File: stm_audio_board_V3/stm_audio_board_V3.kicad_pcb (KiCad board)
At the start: 4 copper layers, 230.9 x 117 mm, 334 parts, among them J1 Power conn, J10 USB_A, J11 AudioJack_Loop1_Return, J12 AudioJack_Loop1_Send, J13 AudioJack_INPUT_Main, J14 AudioJack_OUTPUT_Main, J15 AudioJack_Loop2_Send, J16 STlink_DISP_MCU, J17 Conn_01x10_Footswitch, J18 USB3_A, J2 STlink_DSP, J3 Audio_sig, J4 Conn_01x01_taptempo, J5 Barrel_Jack_MountingPin, J6 Conn_01x03_pot_ext, J7 AudioJack_Loop3_Return, J8 AudioJack_Loop3_Send, J9 AudioJack_Loop2_Return, SW1 SW_SPST, SW2 SW_SPST, U1 IS42S16100H-7TL, U10 OP275, U12 OP275, U13 74HC14, U14 OP275, U15 STM32H723ZGTx, U2 OP275, U3 7909, U4 OP275, U5 MIC2920A-3.3WS-TR, U6 7809, U7 STM32H723ZGTx, U8 OP275, U9 MIC2920A-3.3WS-TR, Y1 X1E0000210132, Y2 X1E0000210132

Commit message: New orientation, Overvoltage protection added
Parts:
- removed C54, C55, C56, C57, C59, C61, C62: 100n, Capacitor_SMD:C_0603_1608Metric
- removed J18: USB3_A, Connector_USB:USB3_A_Receptacle_Wuerth_692122030100
- added C63: 100n, Capacitor_SMD:C_0603_1608Metric, F.Cu at (81.6, 126.1)
- added D1: 1N5819, Diode_SMD:D_SOD-323, F.Cu at (218.1, 82.8)
- added D12: 1N5819, Diode_SMD:D_SOD-323, F.Cu at (209.2, 79.0)
- added D13: 1N5819, Diode_SMD:D_SOD-323, F.Cu at (192.4, 84.8)
- added D14: 1N5819, Diode_SMD:D_SOD-323, F.Cu at (189.1, 84.8)
- added D15: 1N5819, Diode_SMD:D_SOD-323, F.Cu at (192.4, 82.8)
- added D16: 1N5819, Diode_SMD:D_SOD-323, F.Cu at (189.1, 82.8)
- added D17: 1N5819, Diode_SMD:D_SOD-323, F.Cu at (200.8, 82.0)
- added D18: 1N5819, Diode_SMD:D_SOD-323, F.Cu at (197.5, 82.0)
- added D19: 1N5819, Diode_SMD:D_SOD-323, F.Cu at (200.8, 80.0)
- added D20: 1N5819, Diode_SMD:D_SOD-323, F.Cu at (197.5, 80.0)
- added D4: 1N5819, Diode_SMD:D_SOD-323, F.Cu at (214.8, 82.8)
- added D5: 1N5819, Diode_SMD:D_SOD-323, F.Cu at (214.8, 80.8)
- added D6: 1N5819, Diode_SMD:D_SOD-323, F.Cu at (218.1, 80.8)
- added D7: 1N5819, Diode_SMD:D_SOD-323, F.Cu at (206.9, 82.4)
- added D8: 1N5819, Diode_SMD:D_SOD-323, F.Cu at (206.9, 79.1)
- added D9: 1N5819, Diode_SMD:D_SOD-323, F.Cu at (209.1, 82.4)
- added U16: USBLC6-2P6, Package_TO_SOT_SMD:SOT-666, F.Cu at (78.5, 126.1)
- moved C129 87.6 mm to (84.8, 91.9), turned to 180 degrees
- moved C131 82.2 mm to (85.0, 110.3), turned to 180 degrees
- moved C127 69.4 mm to (104.7, 92.1), turned to 180 degrees
- moved C130 62.7 mm to (105.1, 109.9), turned to 180 degrees
- moved C126 57.4 mm to (124.8, 92.0), turned to 180 degrees
- moved C78 54.0 mm to (170.0, 130.7), turned to -90 degrees
- moved C188 53.6 mm to (247.3, 128.9)
- moved C189 53.6 mm to (245.0, 121.6)
- moved J17 53.6 mm to (234.7, 142.4)
- moved R78 53.6 mm to (235.6, 124.7)
- moved C185 53.6 mm to (238.1, 122.5)
- moved C186 53.6 mm to (238.2, 125.6)
- moved C187 53.6 mm to (238.2, 129.2)
- moved R33 53.6 mm to (239.6, 134.2)
- moved R75 53.6 mm to (235.6, 123.1)
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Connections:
- J10 pad 1: unconnected-(J10-VBUS-Pad1) -> +3.3V
- J10 pad 2: unconnected-(J10-D--Pad2) -> /MCU/USB_Conn_D-
- J10 pad 3: unconnected-(J10-D+-Pad3) -> /MCU/USB_Conn_D+
- J10 pad 4: unconnected-(J10-GND-Pad4) -> GND
- U15 pad 102: unconnected-(U15-PA10-Pad102) -> DSP_USB_HS_ID
- U15 pad 103: unconnected-(U15-PA11-Pad103) -> DSP_USB_HS_DM
- U15 pad 104: unconnected-(U15-PA12-Pad104) -> DSP_USB_HS_DP
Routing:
- net -9V: track 235.9 -> 109.7 mm, vias 8 -> 6
- net +3.3VA: track 20.5 -> 69.1 mm, vias 0 -> 8
- net DSP_USB_HS_DP: track 38.5 -> 0.00 mm
- net DSP_USB_HS_DM: track 36.6 -> 0.00 mm
- net /MCU/NRST: track 33.3 -> 0.00 mm
- net +3.3V: track 114.6 -> 98.4 mm
- net AD1939_CM: track 217.0 -> 210.0 mm
- net AD1939_SAI1B_SDI: track 9.20 -> 14.6 mm
- net AD1939_SAI1A_CK: track 15.8 -> 20.3 mm
- net AD1939_SAI1A_WS: track 15.7 -> 19.6 mm
- net AD1939_SAI1A_SDO: track 11.6 -> 15.4 mm
- net AD1939_FILTR: track 5.81 -> 9.56 mm
- net /MCU/USB_Conn_D-: track 0.00 -> 3.36 mm
- net /MCU/USB_Conn_D+: track 0.00 -> 3.25 mm
- net ADC2P: track 25.8 -> 27.6 mm
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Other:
- board text removed: "C50"
- board text removed: "R5"
- board text removed: "R9"
- board text removed: "TapTempo"

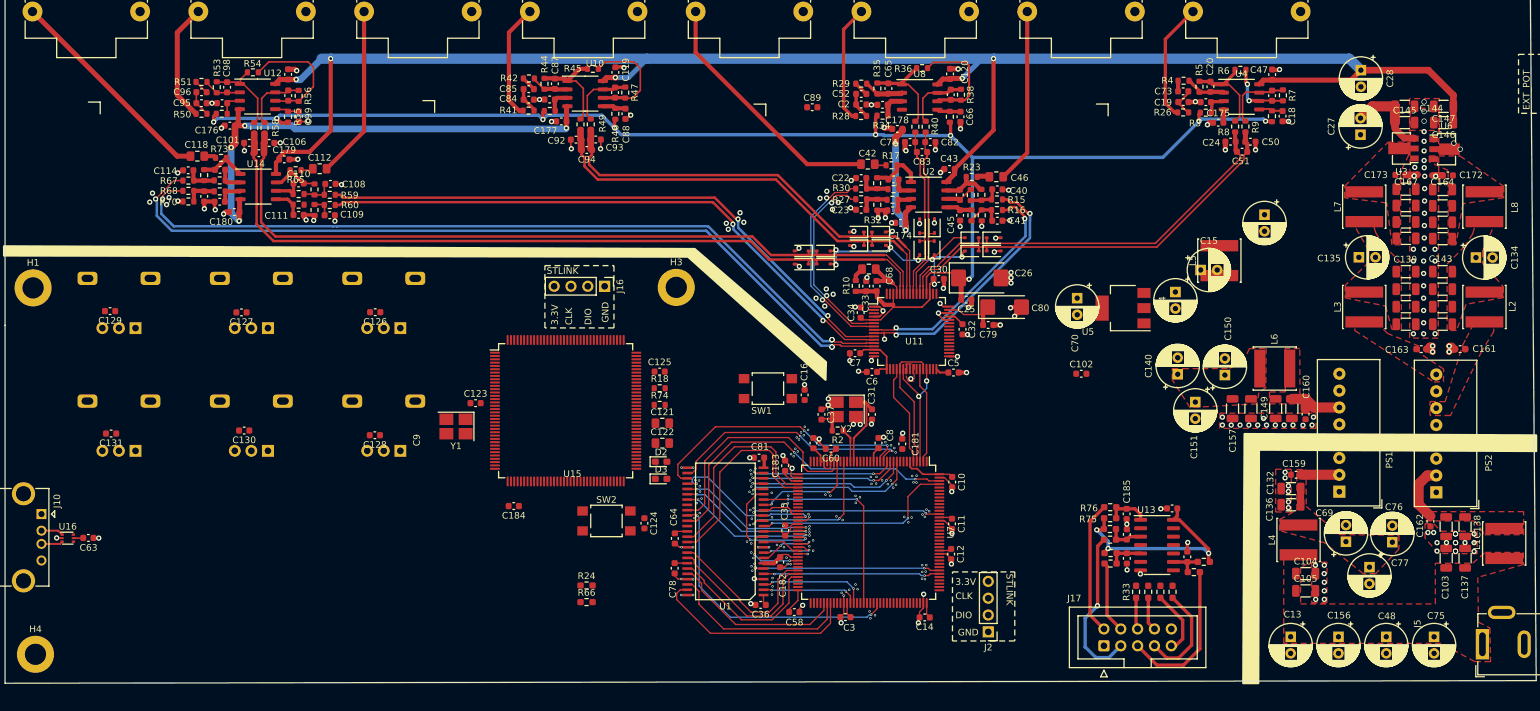
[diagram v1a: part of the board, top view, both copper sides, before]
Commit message: Testpoints and parts for usb hub added
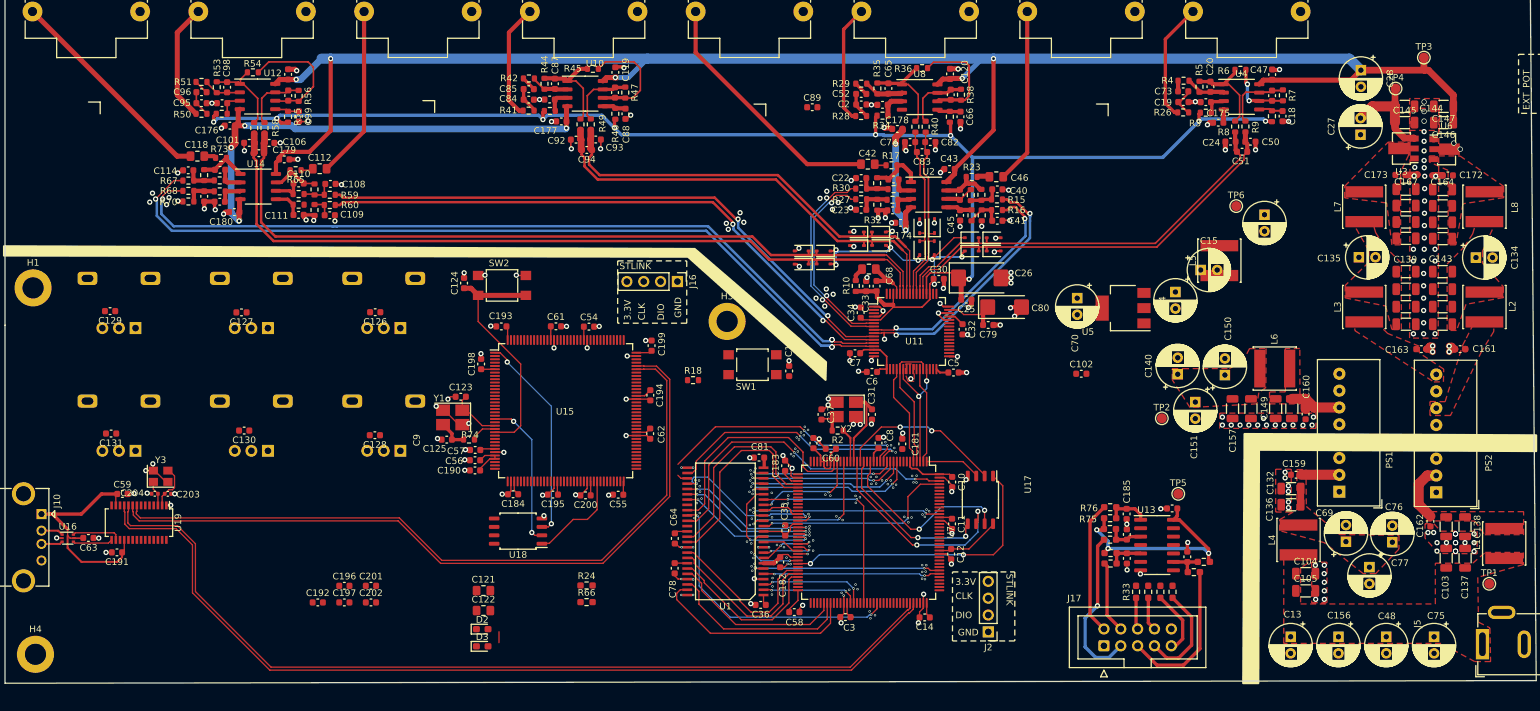
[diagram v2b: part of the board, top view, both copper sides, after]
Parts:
- added C190: 100n, Capacitor_SMD:C_0603_1608Metric, F.Cu at (139.9, 115.9)
- added C191: 100n, Capacitor_SMD:C_0603_1608Metric, F.Cu at (85.9, 128.3)
- added C192: 100n, Capacitor_SMD:C_0603_1608Metric, F.Cu at (116.2, 135.8)
- added C193: 100n, Capacitor_SMD:C_0603_1608Metric, F.Cu at (143.8, 94.2)
- added C194: 100n, Capacitor_SMD:C_0603_1608Metric, F.Cu at (166.3, 104.6)
- added C195: 100n, Capacitor_SMD:C_0603_1608Metric, F.Cu at (151.6, 119.5)
- added C196: 100n, Capacitor_SMD:C_0603_1608Metric, F.Cu at (120.2, 133.3)
- added C197: 100n, Capacitor_SMD:C_0603_1608Metric, F.Cu at (120.2, 135.8)
- added C198: 100n, Capacitor_SMD:C_0603_1608Metric, F.Cu at (140.8, 99.9)
- added C199: 100n, Capacitor_SMD:C_0603_1608Metric, F.Cu at (166.5, 97.1)
- added C200: 100n, Capacitor_SMD:C_0603_1608Metric, F.Cu at (156.5, 119.7)
- added C201: 100n, Capacitor_SMD:C_0603_1608Metric, F.Cu at (124.2, 133.3)
- added C202: 100n, Capacitor_SMD:C_0603_1608Metric, F.Cu at (124.2, 135.8)
- added C203: 20P, Capacitor_SMD:C_0402_1005Metric, F.Cu at (93.6, 119.4)
- added C204: 20P, Capacitor_SMD:C_0402_1005Metric, F.Cu at (91.6, 119.4)
- added C54: 100n, Capacitor_SMD:C_0603_1608Metric, F.Cu at (157.1, 94.2)
- added C55: 100n, Capacitor_SMD:C_0603_1608Metric, F.Cu at (161.5, 119.6)
- added C56: 100n, Capacitor_SMD:C_0603_1608Metric, F.Cu at (139.9, 114.4)
- added C57: 100n, Capacitor_SMD:C_0603_1608Metric, F.Cu at (139.9, 112.8)
- added C59: 100n, Capacitor_SMD:C_0603_1608Metric, F.Cu at (86.7, 119.5)
- added C61: 100n, Capacitor_SMD:C_0603_1608Metric, F.Cu at (152.1, 94.2)
- added C62: 100n, Capacitor_SMD:C_0603_1608Metric, F.Cu at (166.3, 110.4)
- added TP1: TestPoint_PWR_IN, TestPoint:TestPoint_Pad_D1.5mm, F.Cu at (292.8, 133.0)
- added TP2: TestPoint_5V, TestPoint:TestPoint_Pad_D1.5mm, F.Cu at (243.4, 108.1)
- added TP3: TestPoint_9V, TestPoint:TestPoint_Pad_D1.5mm, F.Cu at (283.0, 53.6)
- added TP4: TestPoint_-9V, TestPoint:TestPoint_Pad_D1.5mm, F.Cu at (278.7, 58.3)
- added TP5: TestPoint_3V3, TestPoint:TestPoint_Pad_D1.5mm, F.Cu at (245.9, 119.4)
- added TP6: TestPoint_3V3A, TestPoint:TestPoint_Pad_D1.5mm, F.Cu at (254.7, 76.0)
- added U17: W25Q128JVS, Package_SO:SOIC-8_5.23x5.23mm_P1.27mm, F.Cu at (216.1, 120.3)
- added U18: W25Q128JVS, Package_SO:SOIC-8_5.23x5.23mm_P1.27mm, F.Cu at (146.4, 125.1)
- added U19: FE1.1s, Package_SO:SSOP-28_3.9x9.9mm_P0.635mm, F.Cu at (89.2, 123.8)
- added Y3: Crystal_GND24, Crystal:Crystal_SMD_3225-4Pin_3.2x2.5mm, F.Cu at (92.5, 116.8)
- moved C124 45.3 mm to (138.2, 87.7), turned to 90 degrees
- moved SW2 38.9 mm to (143.9, 88.0), turned to 180 degrees
- moved C121 36.9 mm to (141.1, 134.0)
- moved C122 36.9 mm to (141.1, 137.0)
- moved D2 36.9 mm to (141.0, 139.8)
- moved D3 36.9 mm to (141.0, 142.4)
- moved C125 33.7 mm to (135.6, 111.3)
- moved R74 29.2 mm to (139.0, 111.2), turned to 180 degrees
- moved J16 11.0 mm to (170.4, 87.4)
- moved H3 9.23 mm to (177.9, 93.4)
- moved R18 5.17 mm to (172.7, 102.3)
- moved SW1 4.30 mm to (181.7, 100.0)
- moved C16 4.30 mm to (187.2, 100.9)
- moved C123 2.43 mm to (137.7, 104.8)
- moved C184 1.78 mm to (145.6, 119.5)
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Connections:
- U15 pad 1: unconnected-(U15-PE2-Pad1) -> /Display_Interface/MCU_Display/DISPLAY_FLASH_D2
- U15 pad 102: DSP_USB_HS_ID -> unconnected-(U15-PA10-Pad102)
- U15 pad 103: DSP_USB_HS_DM -> DISPLAY_USB_HS_D-
- U15 pad 104: DSP_USB_HS_DP -> DISPLAY_USB_HS_D+
- U15 pad 18: unconnected-(U15-PF6-Pad18) -> /Display_Interface/MCU_Display/DISPLAY_FLASH_D3
- U15 pad 20: unconnected-(U15-PF8-Pad20) -> /Display_Interface/MCU_Display/DISPLAY_FLASH_D0
- U15 pad 21: unconnected-(U15-PF9-Pad21) -> /Display_Interface/MCU_Display/DISPLAY_FLASH_D1
- U15 pad 22: unconnected-(U15-PF10-Pad22) -> /Display_Interface/MCU_Display/DISPLAY_FLASH_CLK
- U15 pad 64: unconnected-(U15-PE11-Pad64) -> /Display_Interface/MCU_Display/DISPLAY_FLASH_CS
- U16 pad 4: DSP_USB_HS_DP -> Net-(U19-DMU)
- U16 pad 6: DSP_USB_HS_DM -> Net-(U19-DPU)
- U7 pad 1: unconnected-(U7-PE2-Pad1) -> /MCU/DSP_FLASH_D2
- U7 pad 102: DSP_USB_HS_ID -> unconnected-(U7-PA10-Pad102)
- U7 pad 103: DSP_USB_HS_DM -> DSP_USB_HS_D-
- U7 pad 104: DSP_USB_HS_DP -> DSP_USB_HS_D+
- U7 pad 18: unconnected-(U7-PF6-Pad18) -> /MCU/DSP_FLASH_D3
- U7 pad 20: unconnected-(U7-PF8-Pad20) -> /MCU/DSP_FLASH_D0
- U7 pad 21: unconnected-(U7-PF9-Pad21) -> /MCU/DSP_FLASH_D1
- U7 pad 22: unconnected-(U7-PF10-Pad22) -> /MCU/DSP_FLASH_CLK
- U7 pad 64: unconnected-(U7-PE11-Pad64) -> /MCU/DSP_FLASH_CS
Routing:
- net DSP_USB_HS_D+: track 0.00 -> 139.8 mm
- net DSP_USB_HS_D-: track 0.00 -> 138.4 mm
- net DISPLAY_USB_HS_D+: track 0.00 -> 113.1 mm
- net DISPLAY_USB_HS_D-: track 0.00 -> 110.9 mm
- net +3.3V: track 98.4 -> 172.7 mm
- net GND: track 154.4 -> 205.2 mm, vias 282 -> 316
- net /MCU/DSP_FLASH_CS: track 0.00 -> 43.1 mm, vias 0 -> 2
- net /Display_Interface/MCU_Display/NRST_2: track 0.00 -> 36.4 mm
- net /MCU/DSP_FLASH_CLK: track 0.00 -> 31.8 mm, vias 0 -> 2
- net /Display_Interface/MCU_Display/DISPLAY_FLASH_D2: track 0.00 -> 31.4 mm, vias 0 -> 2
- net /MCU/DSP_FLASH_D3: track 0.00 -> 27.8 mm, vias 0 -> 2
- net /MCU/DSP_FLASH_D1: track 0.00 -> 25.3 mm, vias 0 -> 2
- net /MCU/DSP_FLASH_D0: track 0.00 -> 25.1 mm, vias 0 -> 2
- net /Display_Interface/MCU_Display/DISPLAY_FLASH_D1: track 0.00 -> 22.6 mm, vias 0 -> 2
- net /Display_Interface/MCU_Display/DISPLAY_FLASH_CS: track 0.00 -> 14.7 mm
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
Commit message: Reworked outline for enclosure
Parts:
- added J18: Conn_01x16_ILI9341, Connector_PinHeader_2.54mm:PinHeader_1x16_P2.54mm_Vertical, B.Cu at (129.5, 85.6)
- J11: value AudioJack_Loop1_Return -> AudioJack_LOOP3_SEND
- J12: value AudioJack_Loop1_Send -> AudioJack_LOOP3_RETURN
- J13: value AudioJack_INPUT_Main -> AudioJack_OUTPUT
- J14: value AudioJack_OUTPUT_Main -> AudioJack_INPUT
- J15: value AudioJack_Loop2_Send -> AudioJack_LOOP2_RETURN
- J7: value AudioJack_Loop3_Return -> AudioJack_LOOP1_SEND
- J8: value AudioJack_Loop3_Send -> AudioJack_LOOP1_RETURN
- J9: value AudioJack_Loop2_Return -> AudioJack_LOOP2_SEND
- moved H1 139.3 mm to (211.6, 72.0)
- moved C201 78.0 mm to (202.1, 137.8), turned to 180 degrees
- moved C129 76.8 mm to (154.7, 123.8), turned to -90 degrees
- moved C131 74.8 mm to (158.6, 123.8), turned to -90 degrees
- moved C49 66.6 mm to (208.5, 139.7)
- moved C127 56.1 mm to (150.9, 123.8), turned to -90 degrees
- moved C130 53.4 mm to (156.6, 123.8), turned to -90 degrees
- moved C1 47.2 mm to (187.7, 139.3), turned to 180 degrees
- moved H4 42.8 mm to (116.1, 139.1)
- moved C126 39.9 mm to (149.0, 123.8), turned to -90 degrees
- moved C177 37.8 mm to (115.1, 62.9)
- moved R41 37.3 mm to (110.7, 61.1)
- moved R44 37.3 mm to (113.1, 57.0)
- moved C84 37.3 mm to (110.7, 59.4)
- moved C85 37.3 mm to (110.7, 57.9)
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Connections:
- C112 pad 2: Audio_Loop3_Send -> Audio_Loop2_Send
- C118 pad 2: Audio_Main_Output -> Audio_Loop1_Send
- C42 pad 2: Audio_Loop2_Send -> Audio_Loop3_Send
- C46 pad 2: Audio_Loop1_Send -> Audio_Main_Output
- J11 pad T: Audio_Loop1_Return -> Audio_Loop3_Send
- J12 pad T: Audio_Loop1_Send -> Audio_Loop3_Return
- J13 pad T: Audio_Main_Input -> Audio_Main_Output
- J14 pad T: Audio_Main_Output -> Audio_Main_Input
- J15 pad T: Audio_Loop2_Send -> Audio_Loop2_Return
- J7 pad T: Audio_Loop3_Return -> Audio_Loop1_Send
- J8 pad T: Audio_Loop3_Send -> Audio_Loop1_Return
- J9 pad T: Audio_Loop2_Return -> Audio_Loop2_Send
- R26 pad 1: Audio_Main_Input -> Audio_Loop3_Return
- R27 pad 1: DAC2P -> DAC2N
- R28 pad 1: Audio_Loop1_Return -> Audio_Loop2_Return
- R30 pad 1: DAC2N -> DAC2P
- R41 pad 1: Audio_Loop2_Return -> Audio_Loop1_Return
- R50 pad 1: Audio_Loop3_Return -> Audio_Main_Input
- U11 pad 30: AD1939_SPI3_MOSI -> AD1939_SPI_MOSI
- U11 pad 31: AD1939_SPI3_MISO -> AD1939_SPI_MISO
- U11 pad 34: AD1939_SPI3_CLK -> AD1939_SPI_CLK
- U15 pad 122: unconnected-(U15-PD6-Pad122) -> /Display_Interface/MCU_Display/ILI9341_TOUCH_IRQ
- U15 pad 123: unconnected-(U15-PD7-Pad123) -> /Display_Interface/MCU_Display/ILI9341_TOUCH_MOSI
- U15 pad 124: unconnected-(U15-PG9-Pad124) -> /Display_Interface/MCU_Display/ILI9341_TOUCH_MISO
- U15 pad 125: unconnected-(U15-PG10-Pad125) -> /Display_Interface/MCU_Display/ILI9341_DISPLAY_RESET
- U15 pad 18: /Display_Interface/MCU_Display/DISPLAY_FLASH_D3 -> /Display_Interface/MCU_Display/ILI9341_DISPLAY_CS
- U15 pad 19: unconnected-(U15-PF7-Pad19) -> /Display_Interface/MCU_Display/ILI9341_DISPLAY_CLK
- U15 pad 20: /Display_Interface/MCU_Display/DISPLAY_FLASH_D0 -> /Display_Interface/MCU_Display/ILI9341_DISPLAY_MISO
- U15 pad 21: /Display_Interface/MCU_Display/DISPLAY_FLASH_D1 -> /Display_Interface/MCU_Display/ILI9341_DISPLAY_MOSI
- U15 pad 29: unconnected-(U15-PC3_C-Pad29) -> /Display_Interface/MCU_Display/DISPLAY_FLASH_D0
- U15 pad 35: unconnected-(U15-PA1-Pad35) -> /Display_Interface/MCU_Display/DISPLAY_FLASH_D3
- U15 pad 40: unconnected-(U15-PA4-Pad40) -> /Display_Interface/MCU_Display/ILI9341_TOUCH_CS
- U15 pad 41: unconnected-(U15-PA5-Pad41) -> /Display_Interface/MCU_Display/ILI9341_TOUCH_CLK
- U15 pad 42: unconnected-(U15-PA6-Pad42) -> POT1
- U15 pad 43: unconnected-(U15-PA7-Pad43) -> POT2
- U15 pad 44: unconnected-(U15-PC4-Pad44) -> POT4
- U15 pad 46: unconnected-(U15-PB0-Pad46) -> /Display_Interface/MCU_Display/DISPLAY_FLASH_D1
- U15 pad 47: unconnected-(U15-PB1-Pad47) -> POT3
- U15 pad 49: unconnected-(U15-PF11-Pad49) -> POT5
- U15 pad 50: unconnected-(U15-PF12-Pad50) -> POT6
- U7 pad 110: unconnected-(U7-PA15(JTDI)-Pad110) -> AD1939_SPI_CS
- U7 pad 123: unconnected-(U7-PD7-Pad123) -> AD1939_SPI_MOSI
- U7 pad 126: unconnected-(U7-PG11-Pad126) -> AD1939_SPI_CLK
- U7 pad 42: unconnected-(U7-PA6-Pad42) -> AD1939_SPI_MISO
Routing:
- net +3.3V: track 172.7 -> 422.2 mm, vias 3 -> 6
- net -9V: track 112.4 -> 278.2 mm
- net POT3: track 0.00 -> 135.6 mm
- net POT6: track 0.00 -> 123.2 mm
- net POT2: track 0.00 -> 99.7 mm
- net POT5: track 0.00 -> 87.4 mm
- net POT1: track 0.00 -> 65.6 mm
- net AD1939_CM: track 210.0 -> 266.9 mm
- net POT4: track 0.00 -> 49.6 mm
- net AD1939_SPI_CS: track 0.00 -> 45.2 mm, vias 0 -> 2
- net ADC3P: track 67.1 -> 110.4 mm
- net ADC3N: track 67.1 -> 110.2 mm
- net AD1939_SPI_MISO: track 0.00 -> 39.3 mm, vias 0 -> 2
- net /Display_Interface/MCU_Display/ILI9341_TOUCH_CLK: track 0.00 -> 39.0 mm
- net /Display_Interface/MCU_Display/ILI9341_TOUCH_CS: track 0.00 -> 37.8 mm
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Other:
- board size 230.9 x 117 mm -> 265 x 117 mm
